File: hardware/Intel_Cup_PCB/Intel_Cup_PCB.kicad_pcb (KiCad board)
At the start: 2 copper layers, 80 x 70 mm, 2 parts, among them U1 DRV8833PW

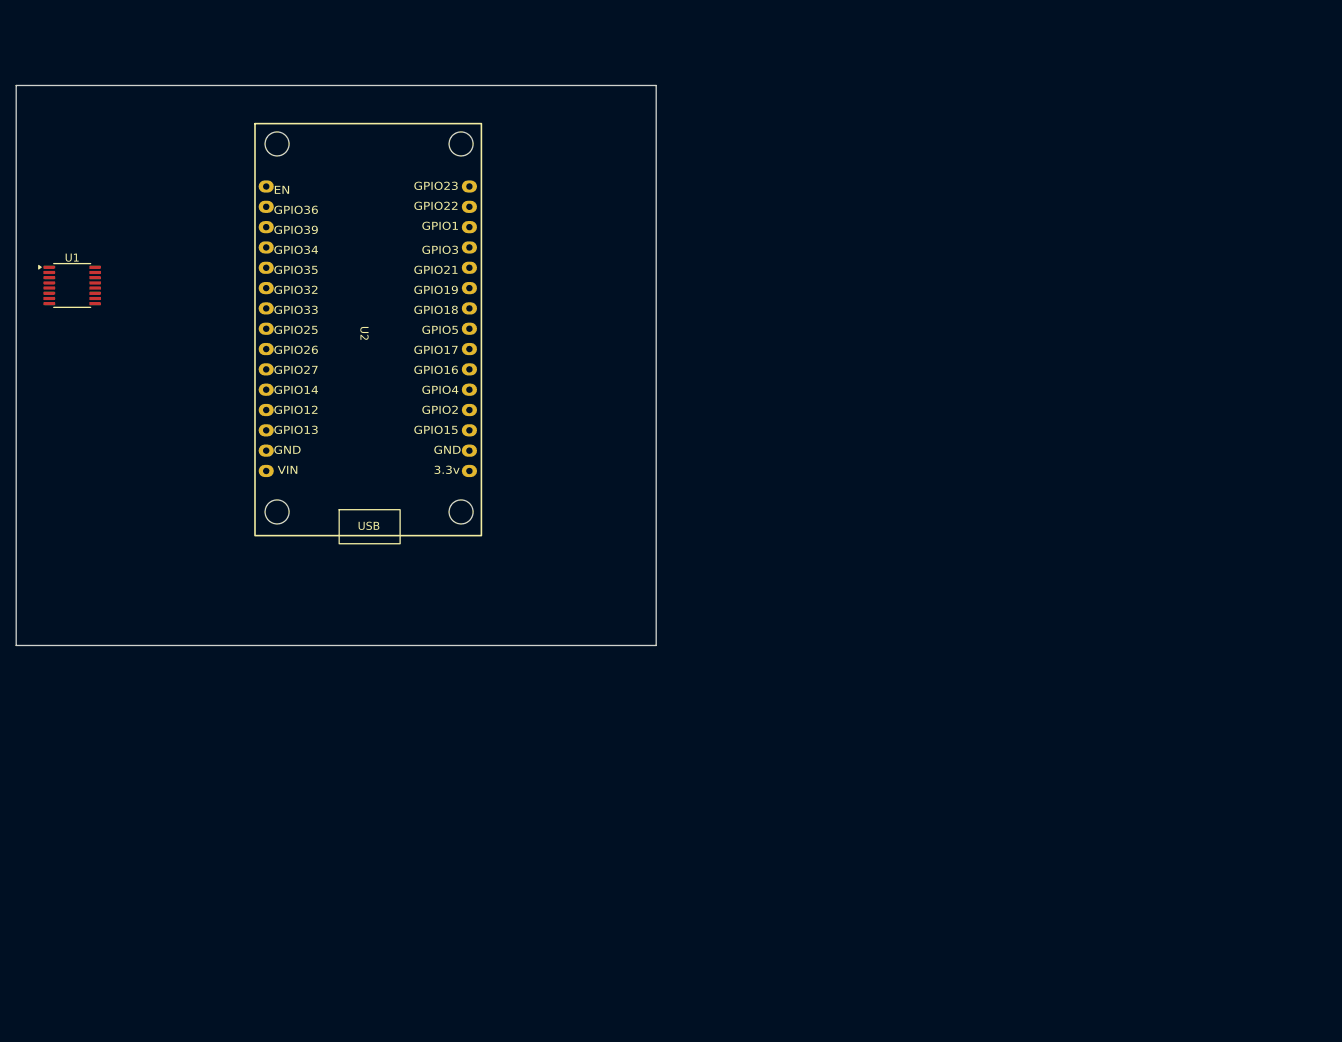
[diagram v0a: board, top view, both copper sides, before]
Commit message: Added footprints for all components(might still need changing) and started PCB placement
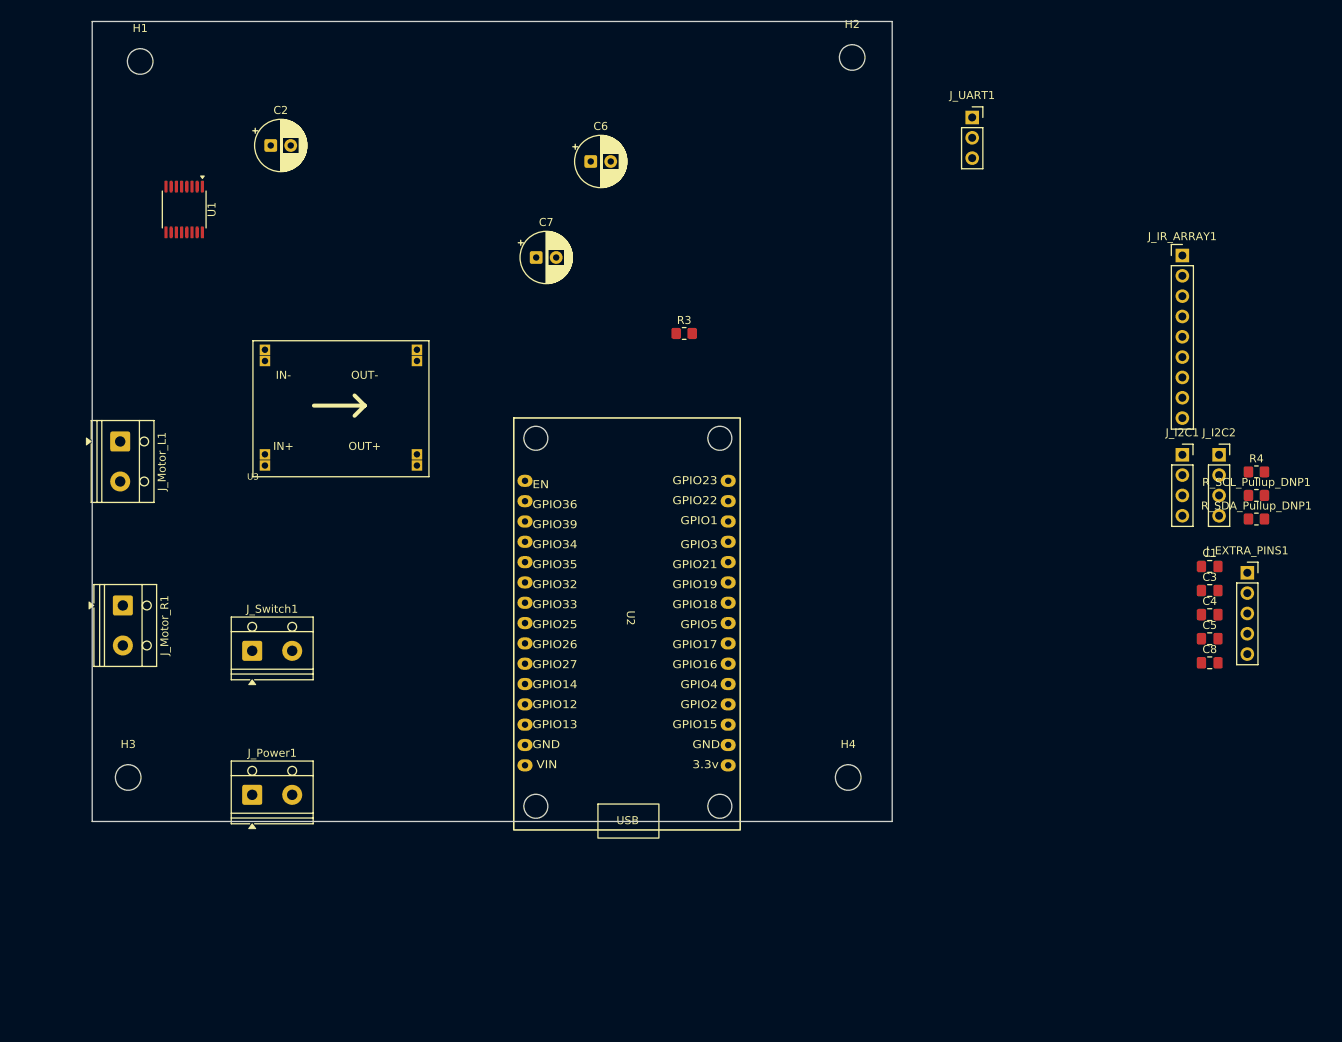
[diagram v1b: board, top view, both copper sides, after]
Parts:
- added C1: 0.1uF, Capacitor_SMD:C_0805_2012Metric_Pad1.18x1.45mm_HandSolder, F.Cu at (249.2, 100.1)
- added C2: 100uF, Capacitor_THT:CP_Radial_D6.3mm_P2.50mm, F.Cu at (131.8, 47.5)
- added C3: 10uF, Capacitor_SMD:C_0805_2012Metric_Pad1.18x1.45mm_HandSolder, F.Cu at (249.2, 103.1)
- added C4: 2.2uF, Capacitor_SMD:C_0805_2012Metric_Pad1.18x1.45mm_HandSolder, F.Cu at (249.2, 106.1)
- added C5: 0.01uF, Capacitor_SMD:C_0805_2012Metric_Pad1.18x1.45mm_HandSolder, F.Cu at (249.2, 109.2)
- added C6: 100uF, Capacitor_THT:CP_Radial_D6.3mm_P2.50mm, F.Cu at (171.8, 49.5)
- added C7: 100uF, Capacitor_THT:CP_Radial_D6.3mm_P2.50mm, F.Cu at (165.0, 61.5)
- added C8: 0.1uF, Capacitor_SMD:C_0805_2012Metric_Pad1.18x1.45mm_HandSolder, F.Cu at (249.2, 112.2)
- added H1: MountingHole, MountingHole:MountingHole_3.2mm_M3, F.Cu at (115.5, 37.0)
- added H2: MountingHole, MountingHole:MountingHole_3.2mm_M3, F.Cu at (204.5, 36.5)
- added H3: MountingHole, MountingHole:MountingHole_3.2mm_M3, F.Cu at (114.0, 126.5)
- added H4: MountingHole, MountingHole:MountingHole_3.2mm_M3, F.Cu at (204.0, 126.5)
- added J_EXTRA_PINS1: Conn_01x05_Pin, Connector_PinSocket_2.54mm:PinSocket_1x05_P2.54mm_Vertical, F.Cu at (253.9, 100.9)
- added J_I2C1: ~, Connector_PinSocket_2.54mm:PinSocket_1x04_P2.54mm_Vertical, F.Cu at (245.8, 86.2)
- added J_I2C2: ~, Connector_PinSocket_2.54mm:PinSocket_1x04_P2.54mm_Vertical, F.Cu at (250.4, 86.2)
- added J_IR_ARRAY1: Conn_01x09_Pin, Connector_PinHeader_2.54mm:PinHeader_1x09_P2.54mm_Vertical, F.Cu at (245.8, 61.3)
- added J_Motor_L1: Conn_01x02_Pin, TerminalBlock_RND:TerminalBlock_RND_205-00012_1x02_P5.00mm_Horizontal, F.Cu at (113.0, 84.5)
- added J_Motor_R1: Conn_01x02_Pin, TerminalBlock_RND:TerminalBlock_RND_205-00012_1x02_P5.00mm_Horizontal, F.Cu at (113.3, 105.0)
- added J_Power1: Conn_01x02_Pin, TerminalBlock_RND:TerminalBlock_RND_205-00012_1x02_P5.00mm_Horizontal, F.Cu at (129.5, 128.7)
- added J_Switch1: Conn_01x02_Pin, TerminalBlock_RND:TerminalBlock_RND_205-00012_1x02_P5.00mm_Horizontal, F.Cu at (129.5, 110.7)
- added J_UART1: ~, Connector_PinSocket_2.54mm:PinSocket_1x03_P2.54mm_Vertical, F.Cu at (219.5, 44.0)
- added R3: 10k, Resistor_SMD:R_0805_2012Metric_Pad1.20x1.40mm_HandSolder, F.Cu at (183.5, 71.0)
- added R4: 10k, Resistor_SMD:R_0805_2012Metric_Pad1.20x1.40mm_HandSolder, F.Cu at (255.0, 88.3)
- added R_SCL_Pullup_DNP1: 4.7k, Resistor_SMD:R_0805_2012Metric_Pad1.20x1.40mm_HandSolder, F.Cu at (255.0, 91.2)
- added R_SDA_Pullup_DNP1: 4.7k, Resistor_SMD:R_0805_2012Metric_Pad1.20x1.40mm_HandSolder, F.Cu at (255.0, 94.2)
- added U3: MP1584, MP1584_Footprint:DC-BRICK, F.Cu at (129.6, 88.9)
- moved U2 49.0 mm to (175.5, 108.0)
- moved U1 16.9 mm to (121.0, 55.5), turned to -90 degrees
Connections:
- U1 pad 12: +5V_MOT -> VBAT_MOT
- U1 pad 13: +5V_MOT -> GND
- U1 pad 3: +5V_MOT -> GND
- U1 pad 6: +5V_MOT -> GND
- U2 pad 17: unconnected-(U2-GND-Pad17) -> GND
- U2 pad 2: +5V_MOT -> GND
- U2 pad 26: Net-(U2-GPIO21) -> /SDA
- U2 pad 29: Net-(U2-GPIO22) -> /SCL
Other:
- board size 80 x 70 mm -> 100 x 100 mm

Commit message: Placement before routing
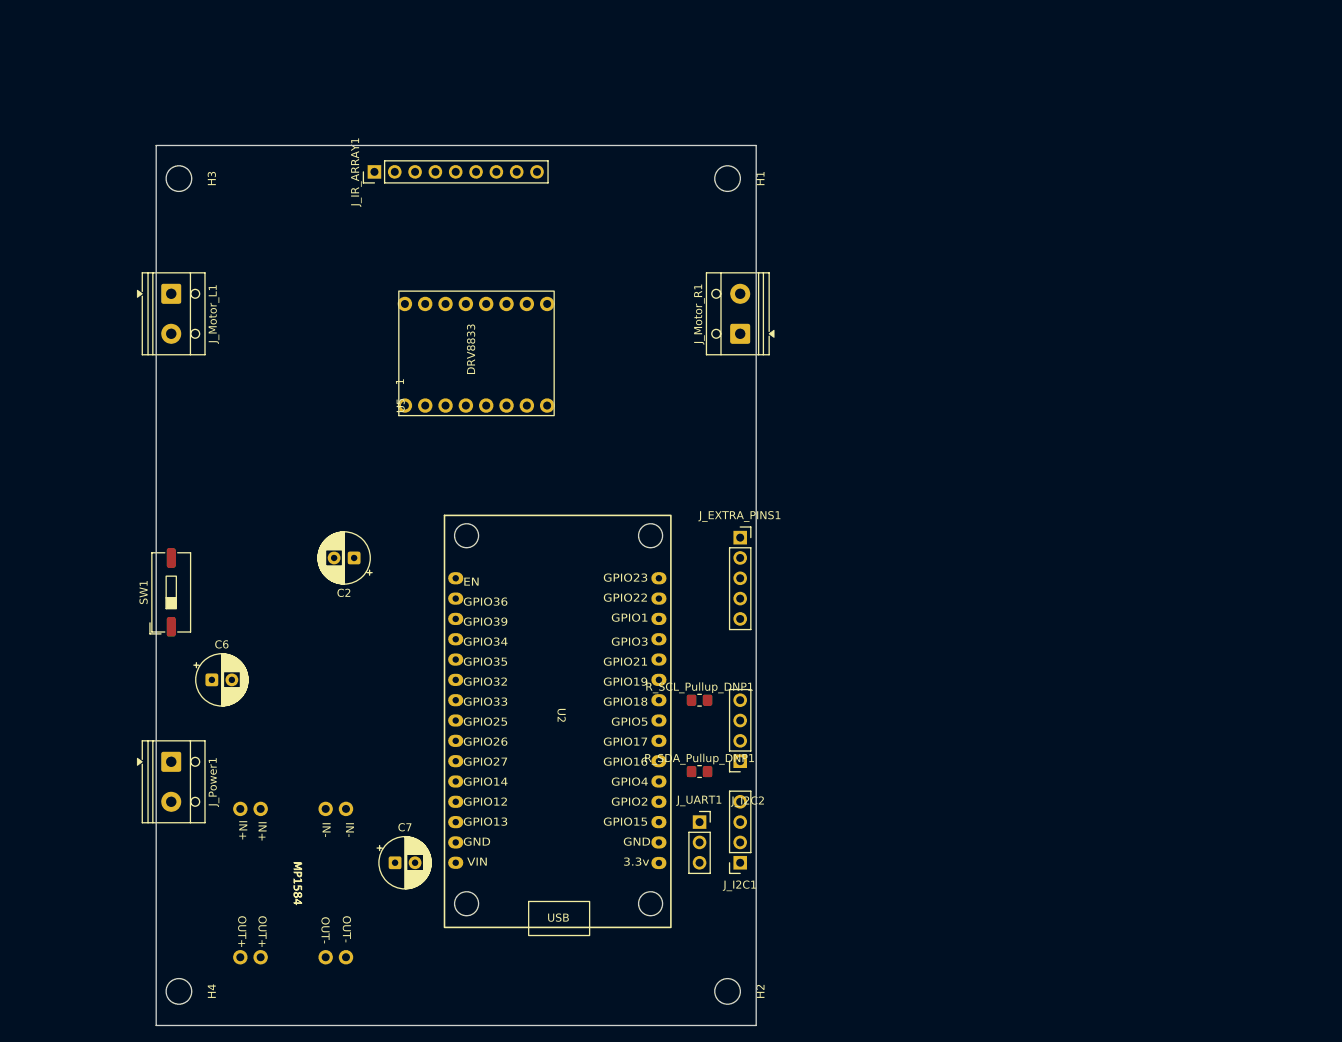
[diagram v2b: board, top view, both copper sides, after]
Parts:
- removed C1, C8: 0.1uF, Capacitor_SMD:C_0805_2012Metric_Pad1.18x1.45mm_HandSolder
- removed C3: 10uF, Capacitor_SMD:C_0805_2012Metric_Pad1.18x1.45mm_HandSolder
- removed C4: 2.2uF, Capacitor_SMD:C_0805_2012Metric_Pad1.18x1.45mm_HandSolder
- removed C5: 0.01uF, Capacitor_SMD:C_0805_2012Metric_Pad1.18x1.45mm_HandSolder
- removed J_Switch1: Conn_01x02_Pin, TerminalBlock_RND:TerminalBlock_RND_205-00012_1x02_P5.00mm_Horizontal
- removed R3, R4: 10k, Resistor_SMD:R_0805_2012Metric_Pad1.20x1.40mm_HandSolder
- removed U1: DRV8833PW, Package_SO:TSSOP-16_4.4x5mm_P0.65mm
- removed U3: MP1584, MP1584_Footprint:DC-BRICK
- added MP1584: ~, intel_cup_footprints:Untitled, F.Cu at (134.6, 139.7)
- added SW1: SW_SPST, Button_Switch_SMD:SW_DIP_SPSTx01_Slide_9.78x4.72mm_W8.61mm_P2.54mm, F.Cu at (119.4, 103.4)
- added U5: ~, intel_cup_footprints:Polulu_DRV8833, F.Cu at (148.6, 80.0)
- moved H2 117.8 mm to (188.9, 153.2), turned to -90 degrees
- moved J_IR_ARRAY1 101.5 mm to (144.8, 50.8), turned to 90 degrees
- moved J_UART1 94.4 mm to (185.4, 132.1)
- moved H4 87.8 mm to (120.3, 153.2), turned to -90 degrees
- moved J_Motor_R1 84.3 mm to (190.5, 71.0), turned to 90 degrees
- moved C6 80.3 mm to (124.5, 114.3)
- moved C7 77.7 mm to (147.4, 137.2)
- moved R_SDA_Pullup_DNP1 76.4 mm to (185.4, 125.8)
- moved J_I2C1 75.2 mm to (190.5, 137.2), turned to 180 degrees
- moved H3 75.1 mm to (120.3, 51.6), turned to -90 degrees
- moved H1 74.9 mm to (188.9, 51.6), turned to -90 degrees
- moved R_SCL_Pullup_DNP1 74.2 mm to (185.4, 116.8)
- moved J_I2C2 71.1 mm to (190.5, 124.5), turned to 180 degrees
- moved J_EXTRA_PINS1 63.5 mm to (190.5, 96.5)
- moved C2 52.6 mm to (142.2, 99.1), turned to 180 degrees
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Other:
- board size 100 x 100 mm -> 75 x 110 mm

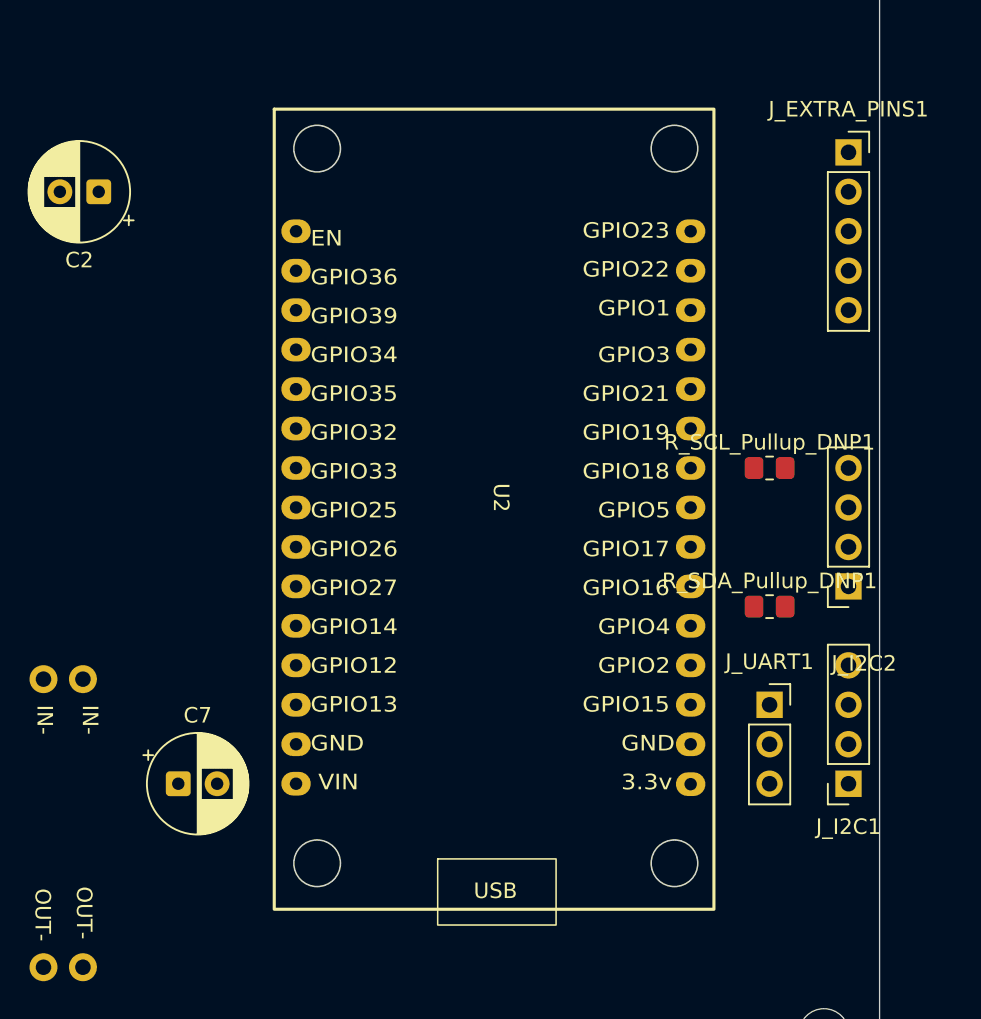
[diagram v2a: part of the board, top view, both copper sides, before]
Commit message: Updated placement, no extra pins
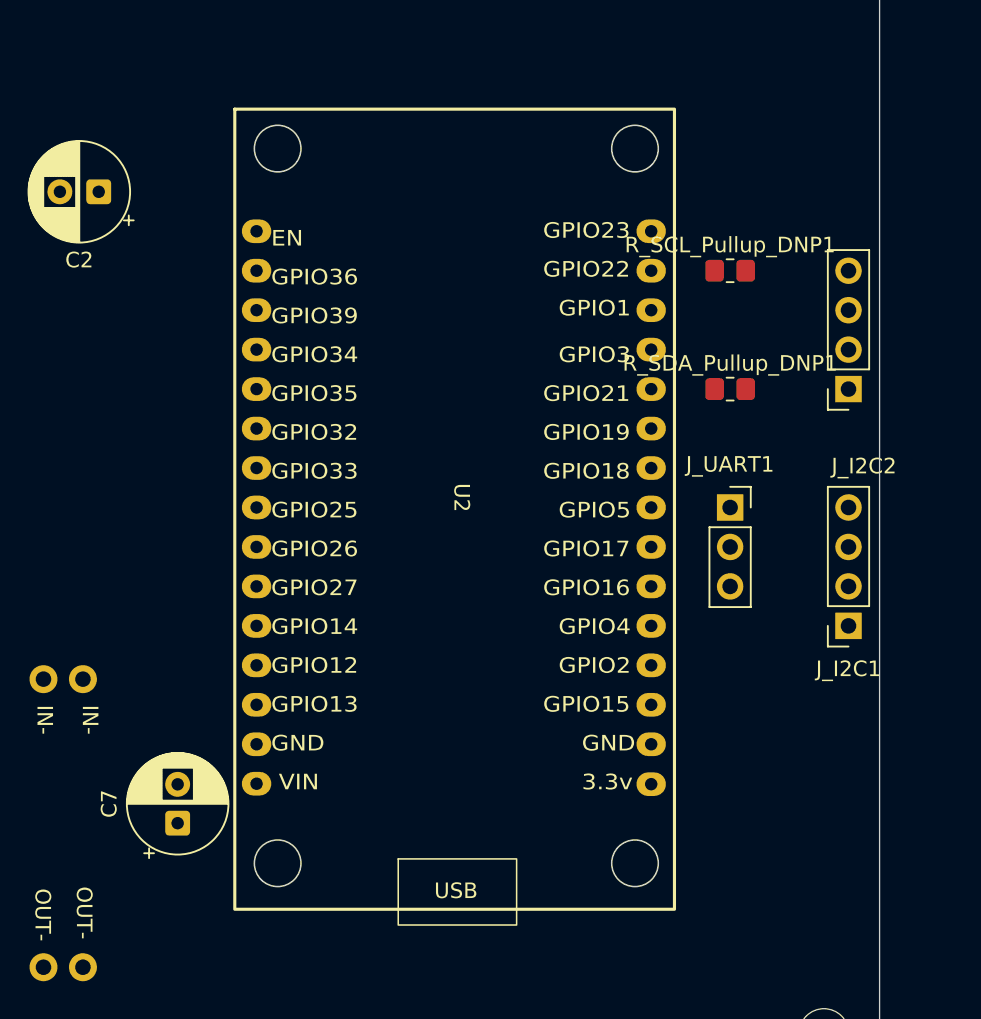
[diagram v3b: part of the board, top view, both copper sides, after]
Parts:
- removed J_EXTRA_PINS1: Conn_01x05_Pin, Connector_PinSocket_2.54mm:PinSocket_1x05_P2.54mm_Vertical
- moved R_SDA_Pullup_DNP1 14.2 mm to (182.9, 111.8)
- moved J_UART1 13.0 mm to (182.9, 119.4)
- moved R_SCL_Pullup_DNP1 13.0 mm to (182.9, 104.1)
- moved J_I2C2 12.7 mm to (190.5, 111.8)
- moved J_I2C1 10.2 mm to (190.5, 127.0)
- moved C7 2.54 mm to (147.3, 139.7), turned to 90 degrees
- moved U2 2.54 mm to (164.3, 120.1)
